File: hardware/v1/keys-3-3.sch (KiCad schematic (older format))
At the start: 10 parts, among them P35 CONN_01X04, P36 CONN_01X08, P37 CONN_01X08, U9 MCP23017

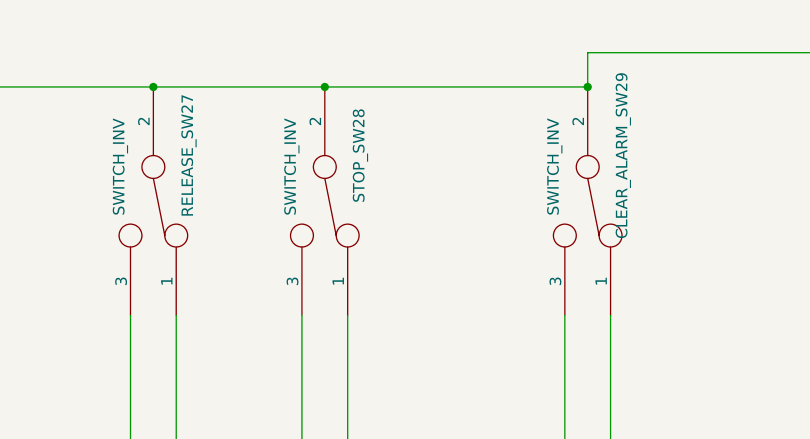
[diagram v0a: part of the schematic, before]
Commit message: Add pcbs and cutouts for magnetic drum store status lamps (not labelled).
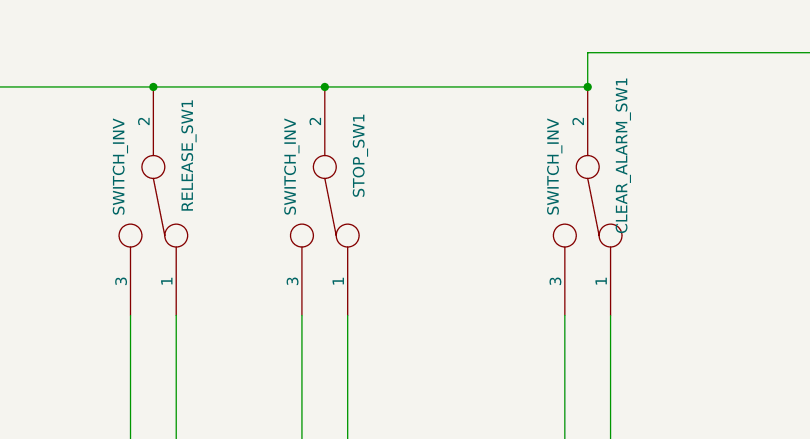
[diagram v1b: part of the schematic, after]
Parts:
- renumbered CLEAR_ALARM_SW29 to CLEAR_ALARM_SW1, RELEASE_SW27 to RELEASE_SW1, STOP_SW28 to STOP_SW1
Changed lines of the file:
@@
 $Descr A4 11693 8268
 encoding utf-8
-Sheet 1 31
+Sheet 1 36
 Title ""
 Date ""
@@
 $EndDescr
 $Comp
-L SWITCH_INV RELEASE_SW27
+L SWITCH_INV RELEASE_SW1
 U 1 1 57AB480A
 P 1600 1900
-F 0 "RELEASE_SW27" H 1400 2050 50  0000 C CNN
+F 0 "RELEASE_SW1" H 1400 2050 50  0000 C CNN
 F 1 "SWITCH_INV" H 1450 1750 50  0000 C CNN
 F 2 "myparts:SW_SPDT-custom" H 1600 1900 50  0001 C CNN
@@
 $EndComp
 $Comp
-L SWITCH_INV STOP_SW28
+L SWITCH_INV STOP_SW1
 U 1 1 57AB4844
 P 2350 1900
-F 0 "STOP_SW28" H 2150 2050 50  0000 C CNN
+F 0 "STOP_SW1" H 2150 2050 50  0000 C CNN
 F 1 "SWITCH_INV" H 2200 1750 50  0000 C CNN
 F 2 "myparts:SW_SPDT-custom" H 2350 1900 50  0001 C CNN
@@
 $EndComp
 $Comp
-L SWITCH_INV CLEAR_ALARM_SW29
+L SWITCH_INV CLEAR_ALARM_SW1
 U 1 1 57AB4869
 P 3500 1900
-F 0 "CLEAR_ALARM_SW29" H 3300 2050 50  0000 C CNN
+F 0 "CLEAR_ALARM_SW1" H 3300 2050 50  0000 C CNN
 F 1 "SWITCH_INV" H 3350 1750 50  0000 C CNN
 F 2 "myparts:SW_SPDT-custom" H 3500 1900 50  0001 C CNN
@@
 Connection ~ 1600 1400
 $Comp
-L GND #PWR01
+L GND #PWR44
 U 1 1 57AB5A9D
 P 700 1550
-F 0 "#PWR01" H 700 1300 50  0001 C CNN
+F 0 "#PWR44" H 700 1300 50  0001 C CNN
 F 1 "GND" H 700 1400 50  0000 C CNN
 F 2 "" H 700 1550 50  0000 C CNN
@@
 $EndComp
 $Comp
-L GND #PWR02
+L GND #PWR48
 U 1 1 57AB5B09
 P 2750 4100
-F 0 "#PWR02" H 2750 3850 50  0001 C CNN
+F 0 "#PWR48" H 2750 3850 50  0001 C CNN
 F 1 "GND" H 2750 3950 50  0000 C CNN
 F 2 "" H 2750 4100 50  0000 C CNN
@@
 NoConn ~ 4050 4450
 $Comp
-L VDD #PWR03
+L VDD #PWR47
 U 1 1 57AB5BBD
 P 2750 3900
-F 0 "#PWR03" H 2750 3750 50  0001 C CNN
+F 0 "#PWR47" H 2750 3750 50  0001 C CNN
 F 1 "VDD" H 2750 4050 50  0000 C CNN
 F 2 "" H 2750 3900 50  0000 C CNN
@@
 NoConn ~ 4050 3750
 $Comp
-L VDD #PWR04
+L VDD #PWR46
 U 1 1 57AB65BE
 P 900 4200
-F 0 "#PWR04" H 900 4050 50  0001 C CNN
+F 0 "#PWR46" H 900 4050 50  0001 C CNN
 F 1 "VDD" H 900 4350 50  0000 C CNN
 F 2 "" H 900 4200 50  0000 C CNN
@@
 $EndComp
 $Comp
-L GND #PWR05
+L GND #PWR45
 U 1 1 57AB65C4
 P 900 3800
-F 0 "#PWR05" H 900 3550 50  0001 C CNN
+F 0 "#PWR45" H 900 3550 50  0001 C CNN
 F 1 "GND" H 900 3650 50  0000 C CNN
 F 2 "" H 900 3800 50  0000 C CNN
@@
 SCK
 $Comp
-L VDD #PWR06
+L VDD #PWR50
 U 1 1 57AB6A0E
 P 5950 4100
-F 0 "#PWR06" H 5950 3950 50  0001 C CNN
+F 0 "#PWR50" H 5950 3950 50  0001 C CNN
 F 1 "VDD" H 5950 4250 50  0000 C CNN
 F 2 "" H 5950 4100 50  0000 C CNN
@@
 Connection ~ 5550 4450
 $Comp
-L GND #PWR07
+L GND #PWR49
 U 1 1 57AB6BD0
 P 5550 4600
-F 0 "#PWR07" H 5550 4350 50  0001 C CNN
+F 0 "#PWR49" H 5550 4350 50  0001 C CNN
 F 1 "GND" H 5550 4450 50  0000 C CNN
 F 2 "" H 5550 4600 50  0000 C CNN
